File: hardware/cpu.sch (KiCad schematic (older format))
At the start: 52 parts

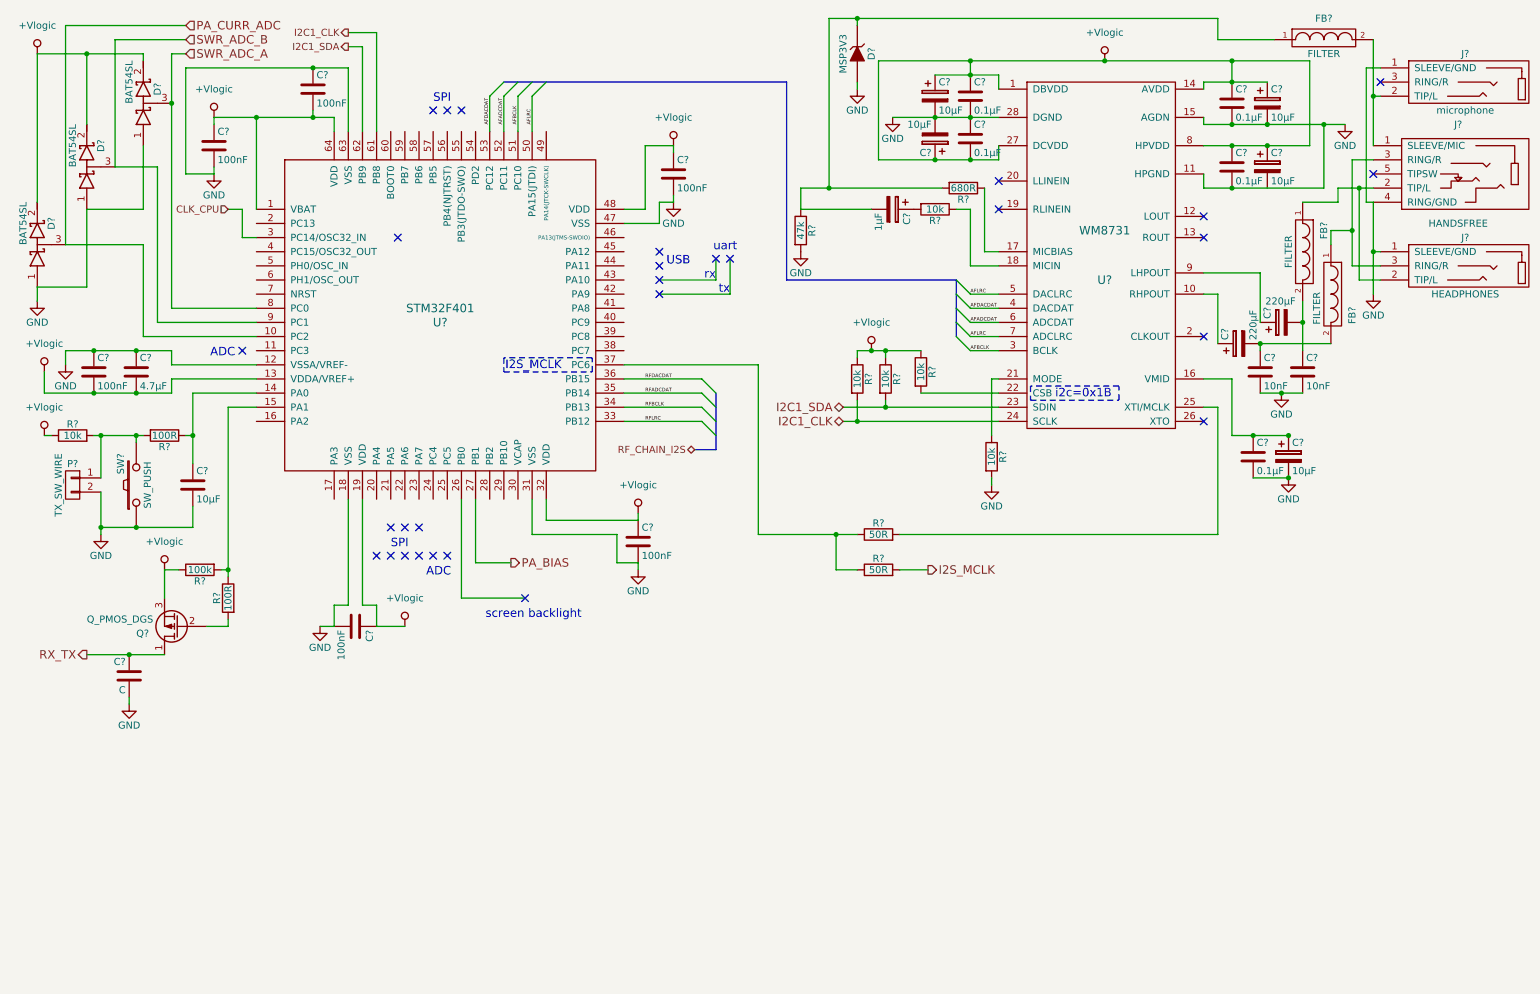
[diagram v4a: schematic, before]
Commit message: added button grid with two pressable rotary encoders for UI block and replotted
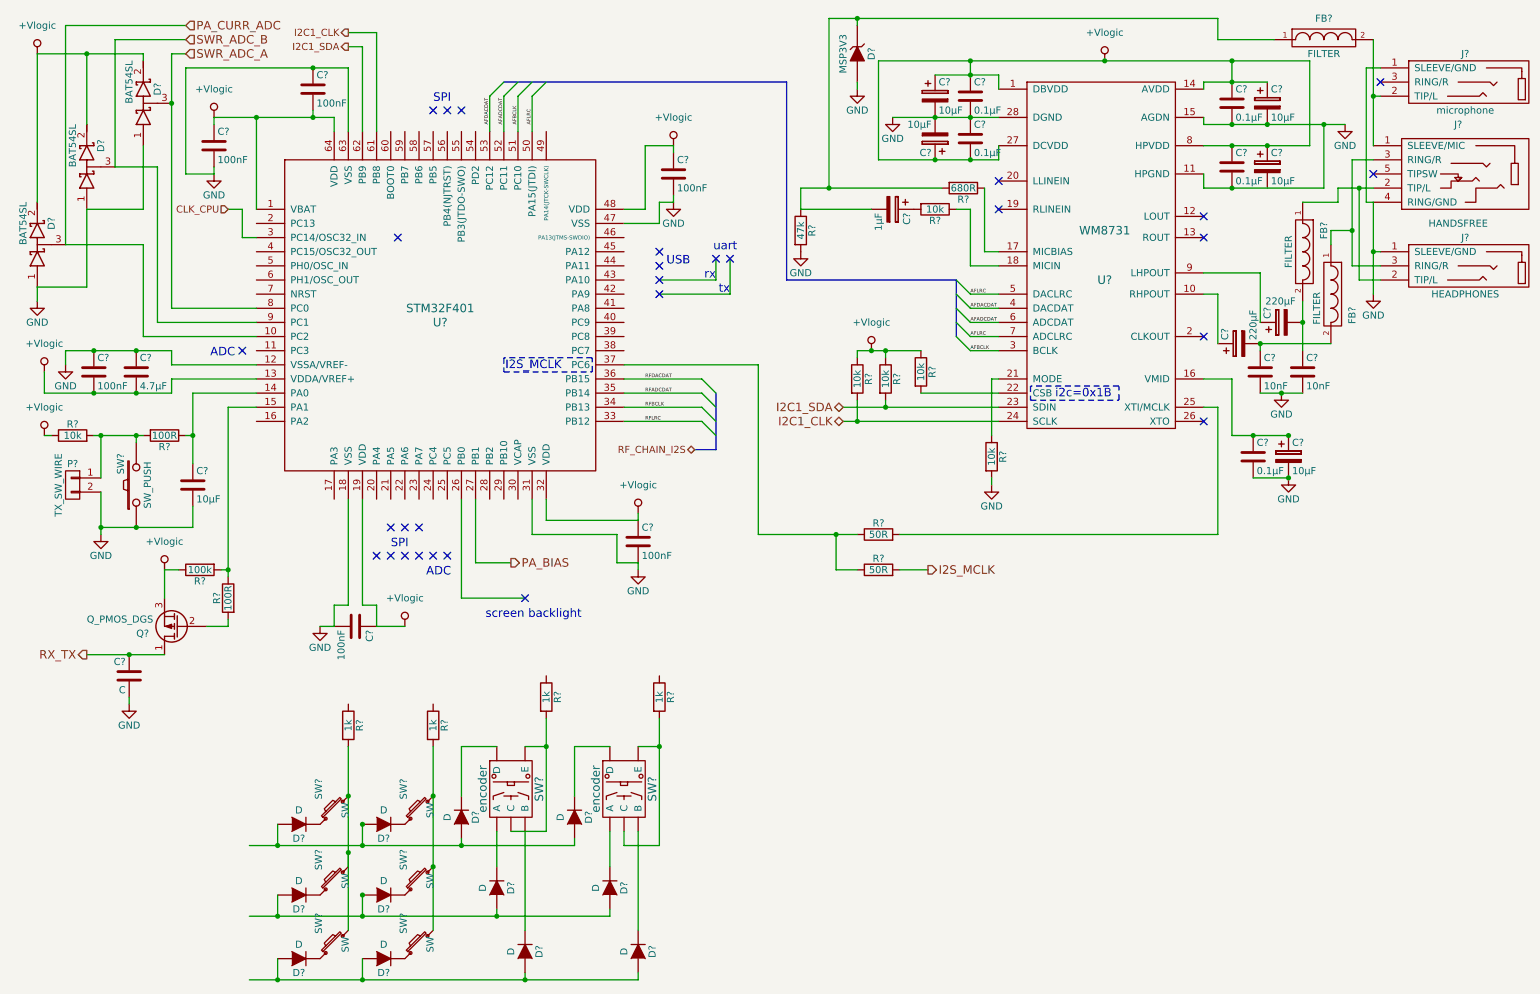
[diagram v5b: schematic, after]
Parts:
- added D? (x12): D, symbol D
- added R? (x4): 1k, symbol R
- added SW? (x6): SW, symbol SW_PUSH_SMALL
- added SW? (x2): encoder, symbol encoder
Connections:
- new net: D?.1 (K), SW?.1 (x6)
- new net: D?.2 (A), D?.2 (A), D?.2 (A), D?.2 (A) (x3)
- new net: R?.2, SW?.2, SW?.2, SW?.2 (x2)
- new net: D?.1 (K), SW?.~ (E) (x6)
- new net: R?.2, SW?.~ (E) (x2)

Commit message: Added annotation so willing prove readers can reference components more easily
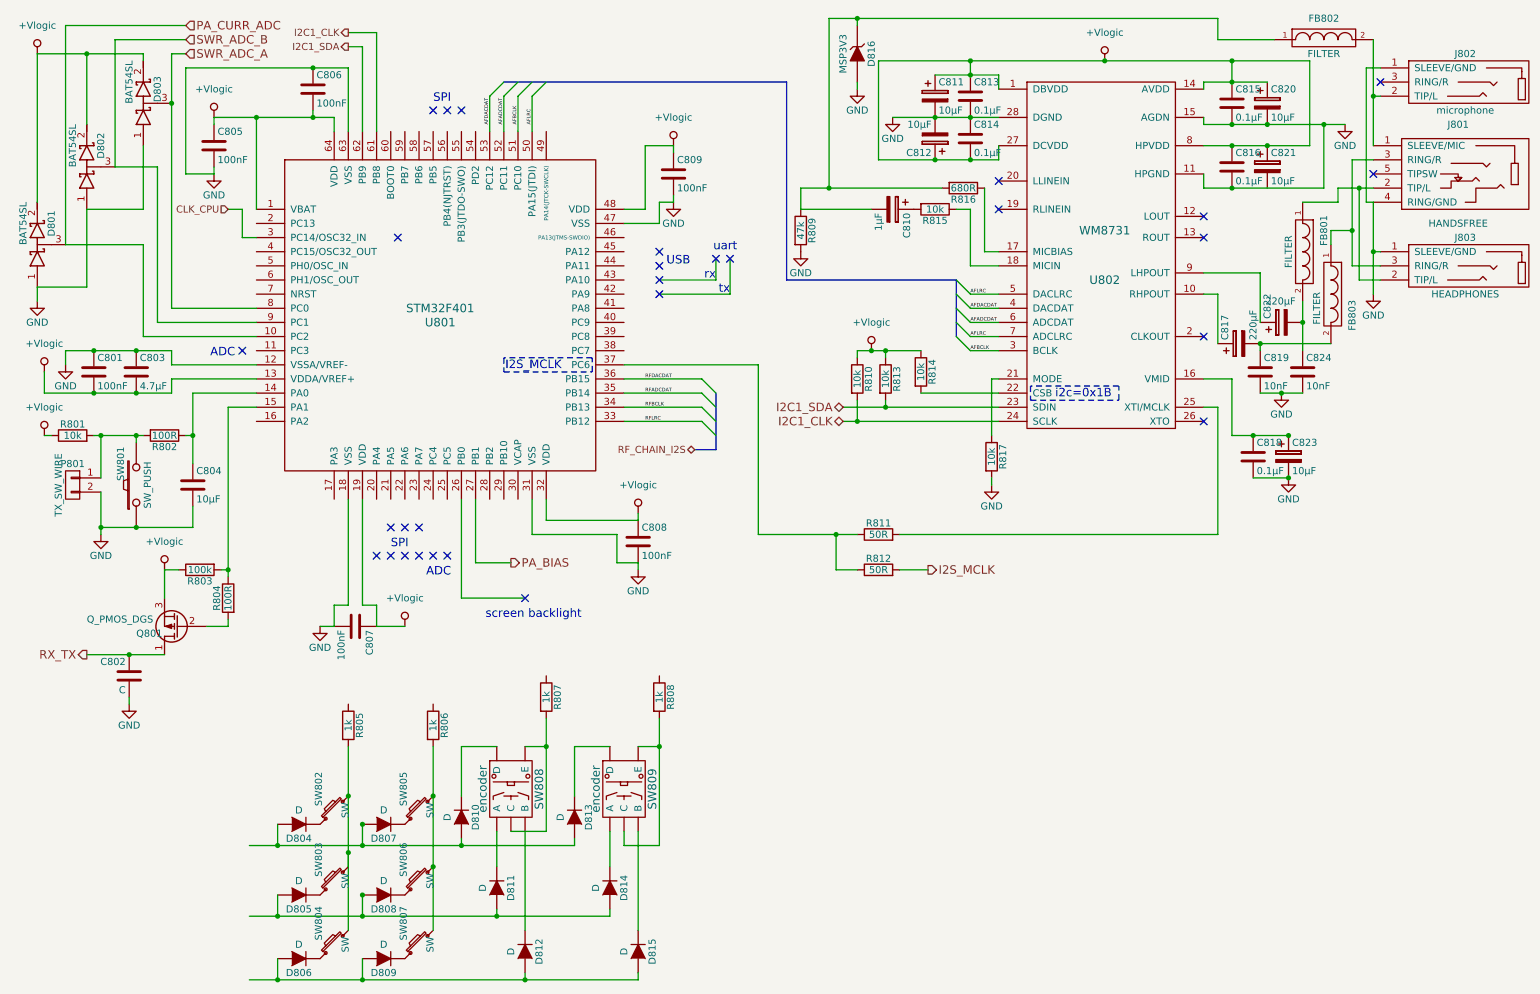
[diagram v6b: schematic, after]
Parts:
- gave numbers to parts that had none: 76

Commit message: fixed some ERC errors
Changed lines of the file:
@@
 $EndComp
 $Comp
-L +Vlogic #PWR809
+L +Vlogic #PWR048
 U 1 1 57E60A73
 P 1900 1250
-F 0 "#PWR809" H 1900 1050 50  0001 C CNN
+F 0 "#PWR048" H 1900 1050 50  0001 C CNN
 F 1 "+Vlogic" H 1900 1450 50  0000 C CNN
 F 2 "" H 1900 1250 50  0000 C CNN
@@
 $EndComp
 $Comp
-L GND #PWR810
+L GND #PWR049
 U 1 1 57E60AA6
 P 1900 1650
-F 0 "#PWR810" H 1900 1400 50  0001 C CNN
+F 0 "#PWR049" H 1900 1400 50  0001 C CNN
 F 1 "GND" H 1900 1500 50  0000 C CNN
 F 2 "" H 1900 1650 50  0000 C CNN
@@
 $EndComp
 $Comp
-L +Vlogic #PWR803
+L +Vlogic #PWR050
 U 1 1 57E60C30
 P 700 3050
-F 0 "#PWR803" H 700 2850 50  0001 C CNN
+F 0 "#PWR050" H 700 2850 50  0001 C CNN
 F 1 "+Vlogic" H 700 3250 50  0000 C CNN
 F 2 "" H 700 3050 50  0000 C CNN
@@
 $EndComp
 $Comp
-L GND #PWR805
+L GND #PWR051
 U 1 1 57E60C66
 P 850 3000
-F 0 "#PWR805" H 850 2750 50  0001 C CNN
+F 0 "#PWR051" H 850 2750 50  0001 C CNN
 F 1 "GND" H 850 2850 50  0000 C CNN
 F 2 "" H 850 3000 50  0000 C CNN
@@
 $EndComp
 $Comp
-L +Vlogic #PWR815
+L +Vlogic #PWR052
 U 1 1 57E60CF4
 P 5150 1450
-F 0 "#PWR815" H 5150 1250 50  0001 C CNN
+F 0 "#PWR052" H 5150 1250 50  0001 C CNN
 F 1 "+Vlogic" H 5150 1650 50  0000 C CNN
 F 2 "" H 5150 1450 50  0000 C CNN
@@
 $EndComp
 $Comp
-L GND #PWR816
+L GND #PWR053
 U 1 1 57E60D4C
 P 5150 1850
-F 0 "#PWR816" H 5150 1600 50  0001 C CNN
+F 0 "#PWR053" H 5150 1600 50  0001 C CNN
 F 1 "GND" H 5150 1700 50  0000 C CNN
 F 2 "" H 5150 1850 50  0000 C CNN
@@
 $EndComp
 $Comp
-L GND #PWR811
+L GND #PWR054
 U 1 1 57E60E1B
 P 2650 4850
-F 0 "#PWR811" H 2650 4600 50  0001 C CNN
+F 0 "#PWR054" H 2650 4600 50  0001 C CNN
 F 1 "GND" H 2650 4700 50  0000 C CNN
 F 2 "" H 2650 4850 50  0000 C CNN
@@
 $EndComp
 $Comp
-L +Vlogic #PWR812
+L +Vlogic #PWR055
 U 1 1 57E60E3B
 P 3250 4850
-F 0 "#PWR812" H 3250 4650 50  0001 C CNN
+F 0 "#PWR055" H 3250 4650 50  0001 C CNN
 F 1 "+Vlogic" H 3250 5050 50  0000 C CNN
 F 2 "" H 3250 4850 50  0000 C CNN
@@
 $EndComp
 $Comp
-L GND #PWR814
+L GND #PWR056
 U 1 1 57E61093
 P 4900 4450
-F 0 "#PWR814" H 4900 4200 50  0001 C CNN
+F 0 "#PWR056" H 4900 4200 50  0001 C CNN
 F 1 "GND" H 4900 4300 50  0000 C CNN
 F 2 "" H 4900 4450 50  0000 C CNN
@@
 $EndComp
 $Comp
-L +Vlogic #PWR813
+L +Vlogic #PWR057
 U 1 1 57E61099
 P 4900 4050
-F 0 "#PWR813" H 4900 3850 50  0001 C CNN
+F 0 "#PWR057" H 4900 3850 50  0001 C CNN
 F 1 "+Vlogic" H 4900 4250 50  0000 C CNN
 F 2 "" H 4900 4050 50  0000 C CNN
@@
 $EndComp
 $Comp
-L +Vlogic #PWR822
+L +Vlogic #PWR058
 U 1 1 57E633B3
 P 8200 850
-F 0 "#PWR822" H 8200 650 50  0001 C CNN
+F 0 "#PWR058" H 8200 650 50  0001 C CNN
 F 1 "+Vlogic" H 8200 1050 50  0000 C CNN
 F 2 "" H 8200 850 50  0000 C CNN
@@
 $EndComp
 $Comp
-L GND #PWR820
+L GND #PWR059
 U 1 1 57E633EA
 P 6700 1250
-F 0 "#PWR820" H 6700 1000 50  0001 C CNN
+F 0 "#PWR059" H 6700 1000 50  0001 C CNN
 F 1 "GND" H 6700 1100 50  0000 C CNN
 F 2 "" H 6700 1250 50  0000 C CNN
@@
 $EndComp
 $Comp
-L GND #PWR825
+L GND #PWR060
 U 1 1 57E6340F
 P 9900 1300
-F 0 "#PWR825" H 9900 1050 50  0001 C CNN
+F 0 "#PWR060" H 9900 1050 50  0001 C CNN
 F 1 "GND" H 9900 1150 50  0000 C CNN
 F 2 "" H 9900 1300 50  0000 C CNN
@@
 NoConn ~ 8900 3400
 $Comp
-L +Vlogic #PWR819
+L +Vlogic #PWR061
 U 1 1 57E6342B
 P 6550 2900
-F 0 "#PWR819" H 6550 2700 50  0001 C CNN
+F 0 "#PWR061" H 6550 2700 50  0001 C CNN
 F 1 "+Vlogic" H 6550 3100 50  0000 C CNN
 F 2 "" H 6550 2900 50  0000 C CNN
@@
 $EndComp
 $Comp
-L GND #PWR824
+L GND #PWR062
 U 1 1 57E6344F
 P 9500 3800
-F 0 "#PWR824" H 9500 3550 50  0001 C CNN
+F 0 "#PWR062" H 9500 3550 50  0001 C CNN
 F 1 "GND" H 9500 3650 50  0000 C CNN
 F 2 "" H 9500 3800 50  0000 C CNN
@@
 $EndComp
 $Comp
-L GND #PWR821
+L GND #PWR063
 U 1 1 57E63F8E
 P 7400 3850
-F 0 "#PWR821" H 7400 3600 50  0001 C CNN
+F 0 "#PWR063" H 7400 3600 50  0001 C CNN
 F 1 "GND" H 7400 3700 50  0000 C CNN
 F 2 "" H 7400 3850 50  0000 C CNN
@@
 $EndComp
 $Comp
-L GND #PWR823
+L GND #PWR064
 U 1 1 57E6E6D8
 P 9450 3200
-F 0 "#PWR823" H 9450 2950 50  0001 C CNN
+F 0 "#PWR064" H 9450 2950 50  0001 C CNN
 F 1 "GND" H 9450 3050 50  0000 C CNN
 F 2 "" H 9450 3200 50  0000 C CNN
@@
 $EndComp
 $Comp
-L GND #PWR826
+L GND #PWR065
 U 1 1 57E705F5
 P 10100 2500
-F 0 "#PWR826" H 10100 2250 50  0001 C CNN
+F 0 "#PWR065" H 10100 2250 50  0001 C CNN
 F 1 "GND" H 10100 2350 50  0000 C CNN
 F 2 "" H 10100 2500 50  0000 C CNN
@@
 $EndComp
 $Comp
-L GND #PWR817
+L GND #PWR066
 U 1 1 57E73E43
 P 6050 2200
-F 0 "#PWR817" H 6050 1950 50  0001 C CNN
+F 0 "#PWR066" H 6050 1950 50  0001 C CNN
 F 1 "GND" H 6050 2050 50  0000 C CNN
 F 2 "" H 6050 2200 50  0000 C CNN
@@
 $EndComp
 $Comp
-L GND #PWR818
+L GND #PWR067
 U 1 1 57E75C81
 P 6450 1050
-F 0 "#PWR818" H 6450 800 50  0001 C CNN
+F 0 "#PWR067" H 6450 800 50  0001 C CNN
 F 1 "GND" H 6450 900 50  0000 C CNN
 F 2 "" H 6450 1050 50  0000 C CNN
@@
 screen backlight
 $Comp
-L +Vlogic #PWR808
+L +Vlogic #PWR068
 U 1 1 57EB8928
 P 1550 4450
-F 0 "#PWR808" H 1550 4250 50  0001 C CNN
+F 0 "#PWR068" H 1550 4250 50  0001 C CNN
 F 1 "+Vlogic" H 1550 4650 50  0000 C CNN
 F 2 "" H 1550 4450 50  0000 C CNN
@@
 $EndComp
 $Comp
-L GND #PWR807
+L GND #PWR069
 U 1 1 57EB8B78
 P 1300 5400
-F 0 "#PWR807" H 1300 5150 50  0001 C CNN
+F 0 "#PWR069" H 1300 5150 50  0001 C CNN
 F 1 "GND" H 1300 5250 50  0000 C CNN
 F 2 "" H 1300 5400 50  0000 C CNN
@@
 $EndComp
 $Comp
-L +Vlogic #PWR804
+L +Vlogic #PWR070
 U 1 1 57EC1B18
 P 700 3500
-F 0 "#PWR804" H 700 3300 50  0001 C CNN
+F 0 "#PWR070" H 700 3300 50  0001 C CNN
 F 1 "+Vlogic" H 700 3700 50  0000 C CNN
 F 2 "" H 700 3500 50  0000 C CNN
@@
 $EndComp
 $Comp
-L GND #PWR806
+L GND #PWR071
 U 1 1 57EC26E5
 P 1100 4200
-F 0 "#PWR806" H 1100 3950 50  0001 C CNN
+F 0 "#PWR071" H 1100 3950 50  0001 C CNN
 F 1 "GND" H 1100 4050 50  0000 C CNN
 F 2 "" H 1100 4200 50  0000 C CNN
@@
 NoConn ~ 3200 2100
 $Comp
-L GND #PWR802
+L GND #PWR072
 U 1 1 57ED45C9
 P 650 2550
-F 0 "#PWR802" H 650 2300 50  0001 C CNN
+F 0 "#PWR072" H 650 2300 50  0001 C CNN
 F 1 "GND" H 650 2400 50  0000 C CNN
 F 2 "" H 650 2550 50  0000 C CNN
@@
 $EndComp
 $Comp
-L +Vlogic #PWR801
+L +Vlogic #PWR073
 U 1 1 57ED529A
 P 650 800
-F 0 "#PWR801" H 650 600 50  0001 C CNN
+F 0 "#PWR073" H 650 600 50  0001 C CNN
 F 1 "+Vlogic" H 650 1000 50  0000 C CNN
 F 2 "" H 650 800 50  0000 C CNN
@@
 	2200 3100 1600 3100
 Wire Wire Line
-	1600 3200 1600 3100
-Wire Wire Line
-	700  3200 1600 3200
+	1600 3100 1600 3200
+Wire Wire Line
+	1600 3200 700  3200
 Wire Wire Line
 	700  3200 700  3050
@@
 Connection ~ 9350 1300
 Wire Wire Line
-	9650 1450 9650 850
-Wire Wire Line
-	8900 1450 9650 1450
+	9650 850  9650 1450
+Wire Wire Line
+	9650 1450 8900 1450
 Connection ~ 9100 850
 Connection ~ 9350 1450
@@
 	4250 5700 4100 5700
 Wire Wire Line
-	5050 6400 4800 6400
-Wire Wire Line
-	5050 5500 5050 6400
+	4800 6400 5050 6400
+Wire Wire Line
+	5050 6400 5050 5500
 Wire Wire Line
 	5050 5700 4900 5700
